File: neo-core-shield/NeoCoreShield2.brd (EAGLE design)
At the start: 49.3 x 46.7 mm, 45 parts, among them J6 BINDER_M12_PAR_8_DIP, J7 BINDER_M12_PAR_8_DIP, J8 BINDER_M12_PAR_8_DIP, J9 BINDER_M12_PAR_8_DIP, Q1 2.5A/30V/105mΩ, Q2 310mA/60V/1.6Ω, Q3 2.5A/30V/105mΩ, Q4 2.5A/30V/105mΩ, Q5 310mA/60V/1.6Ω, Q6 310mA/60V/1.6Ω

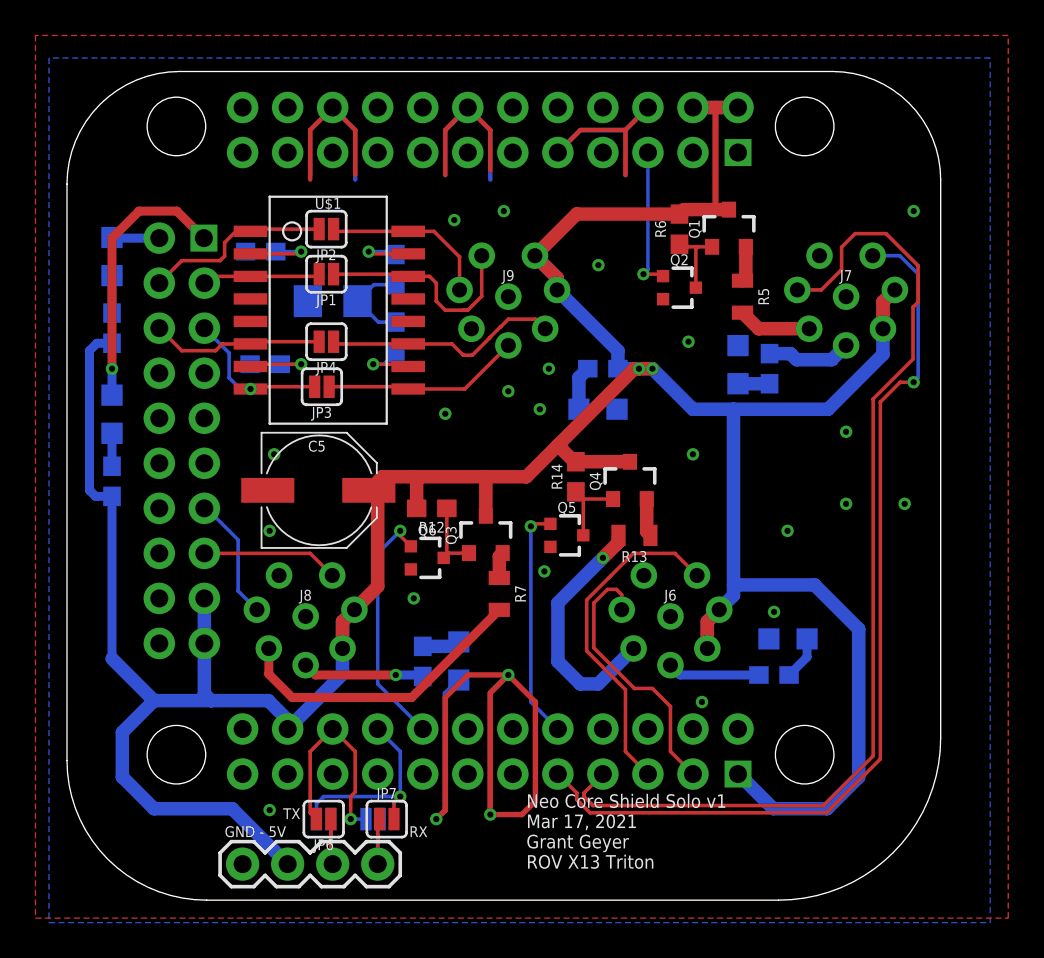
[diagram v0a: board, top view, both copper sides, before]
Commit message: Rectangular layout for holes
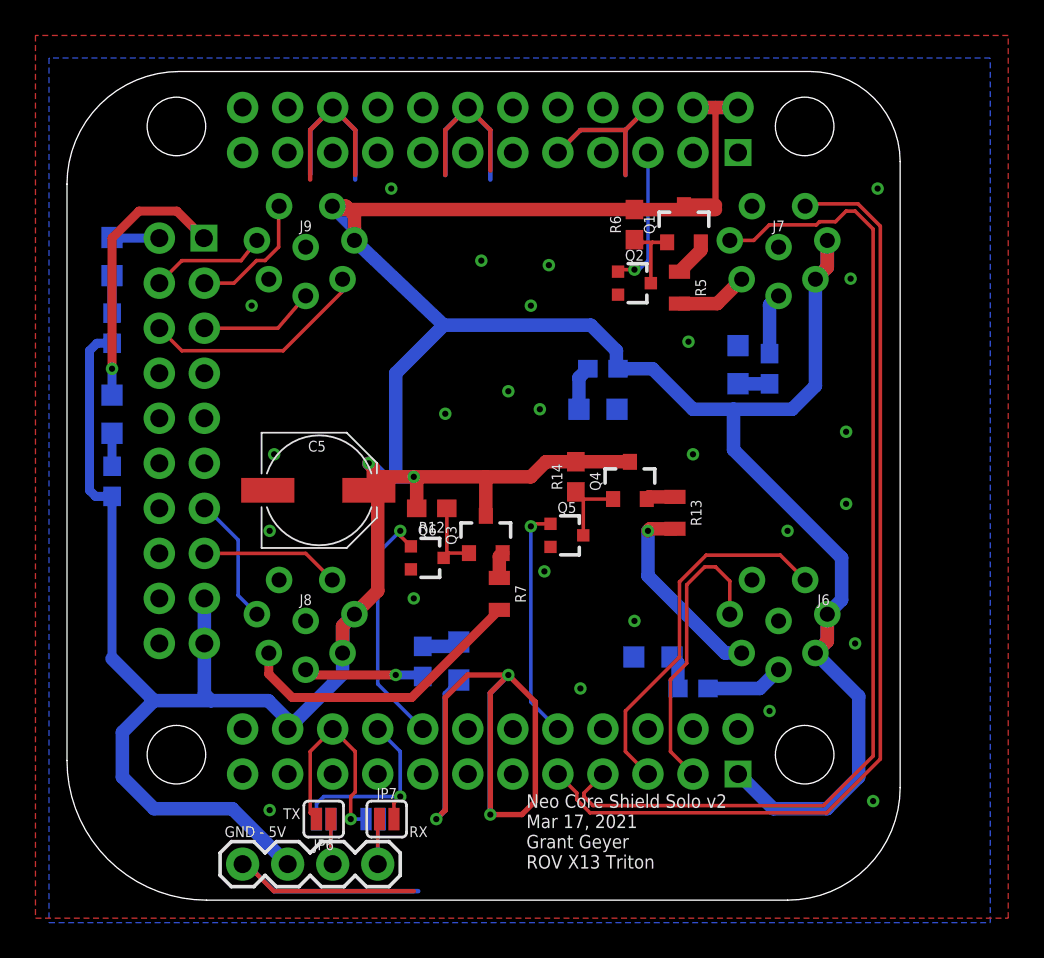
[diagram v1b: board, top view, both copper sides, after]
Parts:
- removed C1, C2: 0.1uF, SparkFun-Capacitors:0603
- removed C3: 1.0nF, SparkFun-Capacitors:1206
- removed JP1, JP2, JP3, JP4: JUMPER-SMT_2_NO_SILK, SparkFun-Jumpers:SMT-JUMPER_2_NO_SILK
- removed R1, R2: 75, SparkFun-Resistors:0603
- removed U$1: ETH-TRANS, ethernet transformer:SOIC-16-WIDE
- moved J9 11.8 mm to (13.5, 36.8)
- moved D6 7.69 mm to (33.0, 13.7)
- moved J6 6.10 mm to (40.1, 15.7)
- moved J7 4.72 mm to (40.1, 36.8)
- moved R11 4.64 mm to (35.3, 11.9), turned to 180 degrees
- moved R5 3.59 mm to (34.5, 34.5)
- moved R13 2.62 mm to (34.3, 21.8), turned to 270 degrees
- moved Q1 2.55 mm to (34.8, 38.1)
- moved Q2 2.55 mm to (32.0, 34.8)
- moved R6 2.55 mm to (32.0, 38.1)
- moved J8 0.25 mm to (13.5, 15.7)
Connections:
- removed net ETH_TD0_GND: C1.1, U$1.7
- removed net ETH_TD1_GND: C2.1, U$1.2
- removed net ETH_TERM_MID: C3.1, R1.2, R2.1
- removed net N$11: R1.1, U$1.15
- removed net N$3: R2.2, U$1.10
- removed net RX_N: J9.6, JP4.1, U$1.11
- removed net RX_P: J9.5, JP3.1, U$1.9
- removed net TX_N: J9.3, JP2.1, U$1.16
- removed net TX_P: J9.2, JP1.1, U$1.14
- net GND: no longer C1.2, C2.2, C3.2
- net RD_N: now also J9.6; no longer JP4.2, U$1.6
- net RD_P: now also J9.5; no longer JP3.2, U$1.8
- net TD_N: now also J9.3; no longer JP2.2, U$1.1
- net TD_P: now also J9.2; no longer JP1.2, U$1.3
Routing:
- net 5V: track 198.2 -> 222.9 mm
- net GND: track 99.2 -> 120.1 mm, vias 24 -> 28
- net RX_N: track 13.3 -> 0.00 mm
- net TX_P: track 12.4 -> 0.00 mm
- net RX_P: track 11.2 -> 0.00 mm
- net TX_N: track 9.62 -> 0.00 mm
- net ETH_TERM_MID: track 5.19 -> 0.00 mm
- net ETH_TD1_GND: track 4.34 -> 0.00 mm, vias 1 -> 0
- net TD_N: track 10.7 -> 6.59 mm
- net ETH_TD0_GND: track 4.09 -> 0.00 mm, vias 1 -> 0
- net N$11: track 3.87 -> 0.00 mm, vias 1 -> 0
- net N$3: track 3.57 -> 0.00 mm, vias 1 -> 0
- net USB_CAM_2_N: track 52.2 -> 55.4 mm, vias 1 -> 0
- net RD_N: track 9.75 -> 12.9 mm
- net LED_1: track 14.2 -> 11.2 mm
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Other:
- board size 49.3 x 46.7 mm -> 47 x 46.7 mm
- board text added: "Neo Core Shield Solo v2 Mar 17, 2021 Grant Geyer ROV X13 Triton"
- board text removed: "Neo Core Shield Solo v1 Mar 17, 2021 Grant Geyer ROV X13 Triton"

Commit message: Square hole pattern order
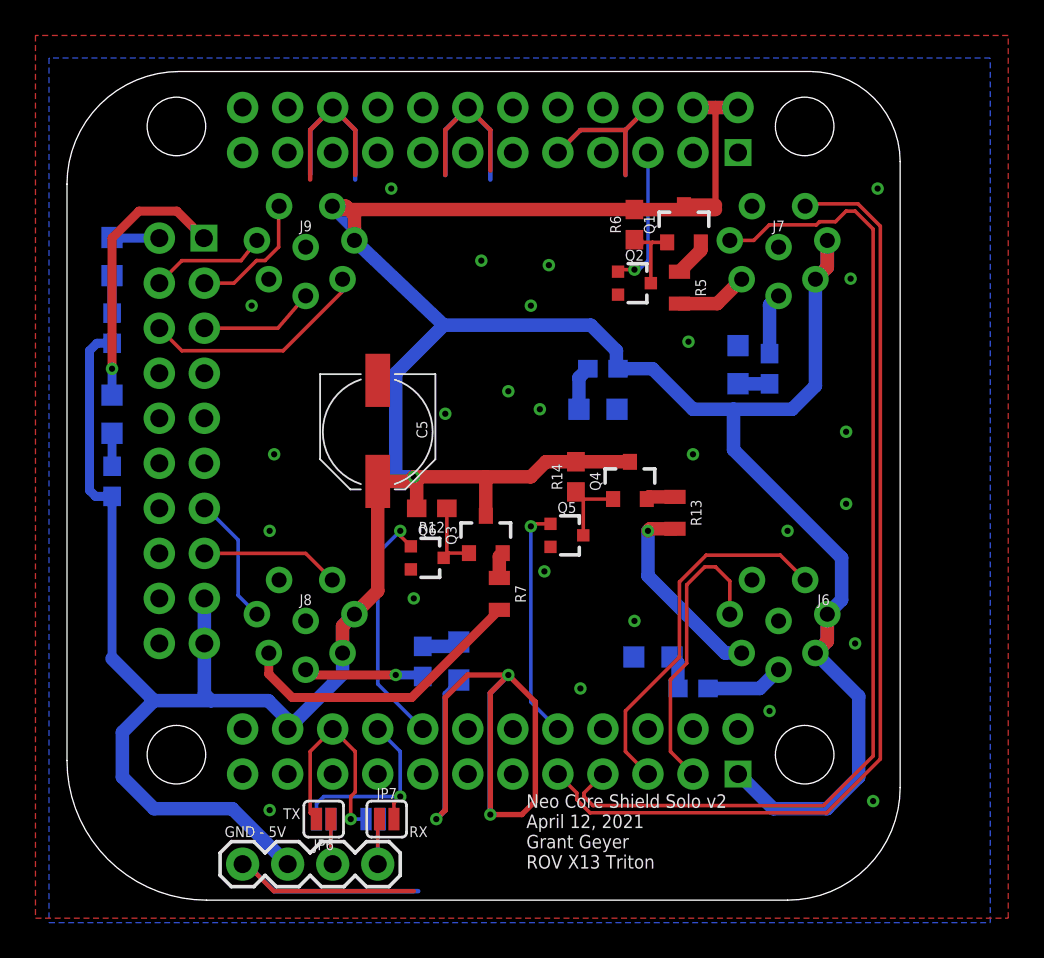
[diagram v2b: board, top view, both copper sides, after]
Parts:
- moved C5 4.67 mm to (17.5, 26.4), turned to 270 degrees
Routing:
- net 5V: track 222.9 -> 219.3 mm, vias 2 -> 1
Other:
- board text added: "Neo Core Shield Solo v2 April 12, 2021 Grant Geyer ROV X13 Triton"
- board text removed: "Neo Core Shield Solo v2 Mar 17, 2021 Grant Geyer ROV X13 Triton"
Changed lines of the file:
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@@
 <wire x1="6.35" y1="46.736" x2="0" y2="40.386" width="0" layer="20" curve="90"/>
 <text x="25.908" y="1.778" size="0.762" layer="25">Neo Core Shield Solo v2
-Mar 17, 2021
+April 12, 2021
 Grant Geyer
 ROV X13 Triton</text>
@@
 <attribute name="VALUE" x="29.464" y="23.876" size="0.6096" layer="27" font="vector" ratio="20" rot="R90" align="top-center"/>
 </element>
-<element name="C5" library="Panasonic 47 uF cap - EEE-1CA470SP" package="PANASONIC_D" package3d_urn="urn:adsk.eagle:package:24384400/2" value="47uF" x="14.224" y="23.114" smashed="yes">
-<attribute name="NAME" x="14.097" y="25.908" size="0.6096" layer="25" font="vector" ratio="20" rot="R180" align="bottom-center"/>
-<attribute name="PROD_ID" value="CAP-08478" x="14.224" y="23.114" size="1.778" layer="27" display="off"/>
-<attribute name="VALUE" x="14.224" y="20.32" size="0.6096" layer="27" font="vector" ratio="20" rot="R180" align="top-center"/>
+<element name="C5" library="Panasonic 47 uF cap - EEE-1CA470SP" package="PANASONIC_D" package3d_urn="urn:adsk.eagle:package:24384400/2" value="47uF" x="17.526" y="26.416" smashed="yes" rot="R270">
+<attribute name="NAME" x="20.32" y="26.543" size="0.6096" layer="25" font="vector" ratio="20" rot="R90" align="bottom-center"/>
+<attribute name="PROD_ID" value="CAP-08478" x="17.526" y="26.416" size="1.778" layer="27" rot="R270" display="off"/>
+<attribute name="VALUE" x="14.732" y="26.416" size="0.6096" layer="27" font="vector" ratio="20" rot="R90" align="top-center"/>
 </element>
 <element name="JP5" library="SparkFun-Jumpers" library_urn="urn:adsk.eagle:library:528" package="SMT-JUMPER_2_NO_SILK" package3d_urn="urn:adsk.eagle:package:39279/1" value="JUMPER-SMT_2_NO_SILK" x="14.478" y="4.572" smashed="yes" rot="MR0">
@@
 <wire x1="31.746" y1="24.726" x2="31.75" y2="24.722" width="0.762" layer="1"/>
 <contactref element="C5" pad="+"/>
-<wire x1="17.786" y1="23.876" x2="17.275" y2="23.365" width="0.762" layer="1"/>
-<wire x1="17.275" y1="23.365" x2="17.024" y2="23.114" width="0.762" layer="1"/>
-<wire x1="19.558" y1="23.876" x2="17.786" y2="23.876" width="0.762" layer="1"/>
-<wire x1="17.526" y1="17.442" x2="17.526" y2="22.612" width="0.762" layer="1"/>
-<wire x1="17.526" y1="22.612" x2="17.024" y2="23.114" width="0.762" layer="1"/>
 <wire x1="16.212" y1="16.128" x2="15.542" y2="15.458" width="0.762" layer="1"/>
 <wire x1="15.542" y1="15.458" x2="15.542" y2="13.938" width="0.762" layer="1"/>
@@
 <wire x1="18.542" y1="23.876" x2="19.558" y2="23.876" width="0.762" layer="16"/>
 <via x="19.558" y="23.876" extent="1-16" drill="0.35"/>
-<wire x1="18.542" y1="23.876" x2="17.78" y2="23.876" width="0.762" layer="16"/>
-<wire x1="17.78" y1="23.876" x2="17.018" y2="24.638" width="0.762" layer="16"/>
-<via x="17.018" y="24.638" extent="1-16" drill="0.35"/>
-<wire x1="17.018" y1="24.638" x2="17.275" y2="24.381" width="0.762" layer="1"/>
-<wire x1="17.275" y1="24.381" x2="17.275" y2="23.365" width="0.762" layer="1"/>
 <wire x1="23.622" y1="23.876" x2="26.162" y2="23.876" width="0.762" layer="1"/>
 <wire x1="26.162" y1="23.876" x2="27.012" y2="24.726" width="0.762" layer="1"/>
@@
 <wire x1="16.212" y1="37.89" x2="14.962" y2="39.14" width="0.762" layer="16"/>
 <wire x1="27.012" y1="24.726" x2="28.702" y2="24.726" width="0.762" layer="1"/>
+<wire x1="19.298" y1="23.616" x2="19.558" y2="23.876" width="0.762" layer="1"/>
+<wire x1="17.526" y1="17.442" x2="17.526" y2="23.616" width="0.762" layer="1"/>
+<wire x1="17.526" y1="23.616" x2="19.298" y2="23.616" width="0.762" layer="1"/>
 </signal>
 <signal name="USB_CAM_2_P" class="1">

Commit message: Flip pinout to be correct
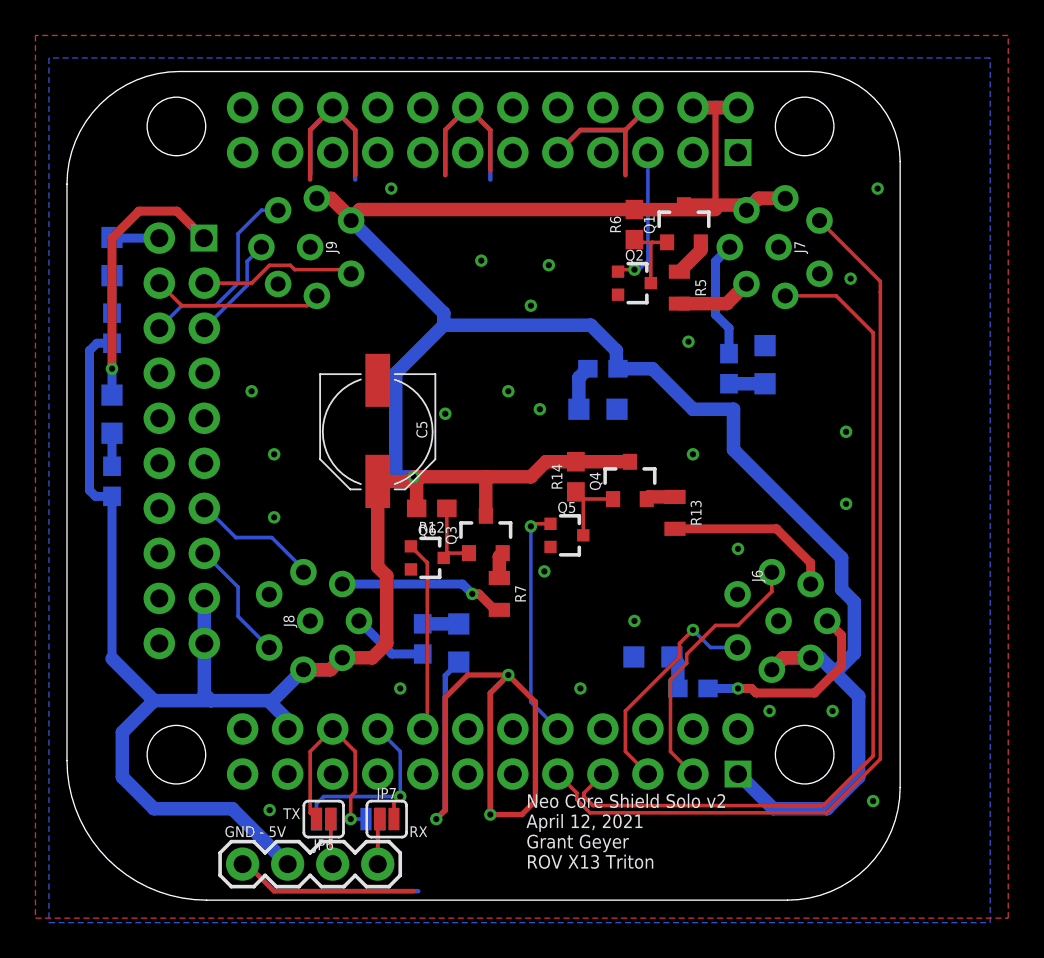
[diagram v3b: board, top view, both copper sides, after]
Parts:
- moved R3 2.29 mm to (37.3, 30.0)
- moved D1 1.52 mm to (39.4, 30.2)
- moved R4 1.27 mm to (20.1, 14.7)
- moved D2 1.02 mm to (22.1, 14.5)
- moved J8 0.25 mm to (13.7, 15.7), turned to 270 degrees
- moved J9 0.25 mm to (13.7, 36.8), turned to 90 degrees
- turned J6 to 270 degrees
- turned J7 to 90 degrees
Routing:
- net USB_CAM_2_P: track 58.3 -> 49.1 mm
- net USB_CAM_1_N: track 20.9 -> 13.2 mm, vias 0 -> 1
- net LED_3: track 16.8 -> 9.46 mm, vias 0 -> 1
- net 5V: track 219.3 -> 212.5 mm
- net CONN_SENSE1: track 4.42 -> 11.1 mm, vias 0 -> 1
- net CONN_SENSE2: track 3.47 -> 6.66 mm
- net USB_CAM_2_N: track 55.4 -> 52.4 mm
- net LED_CONTROL3: track 13.9 -> 10.8 mm, vias 1 -> 0
- net TD_N: track 6.59 -> 9.64 mm
- net CONN_SENSE3: track 6.76 -> 4.37 mm, vias 1 -> 0
- net RD_N: track 12.9 -> 11.1 mm
- net USB_CAM_1_P: track 16.6 -> 15.0 mm
- net LED_1: track 11.2 -> 9.64 mm, vias 1 -> 0
- net TD_P: track 7.35 -> 8.89 mm
- net GND: track 120.1 -> 121.1 mm
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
